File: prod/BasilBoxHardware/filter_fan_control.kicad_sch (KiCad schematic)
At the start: 4 parts, among them J1 FAN, U3 DEBO_Relais, U5 DEBO_Mosfet, U6 DEBO_Mosfet

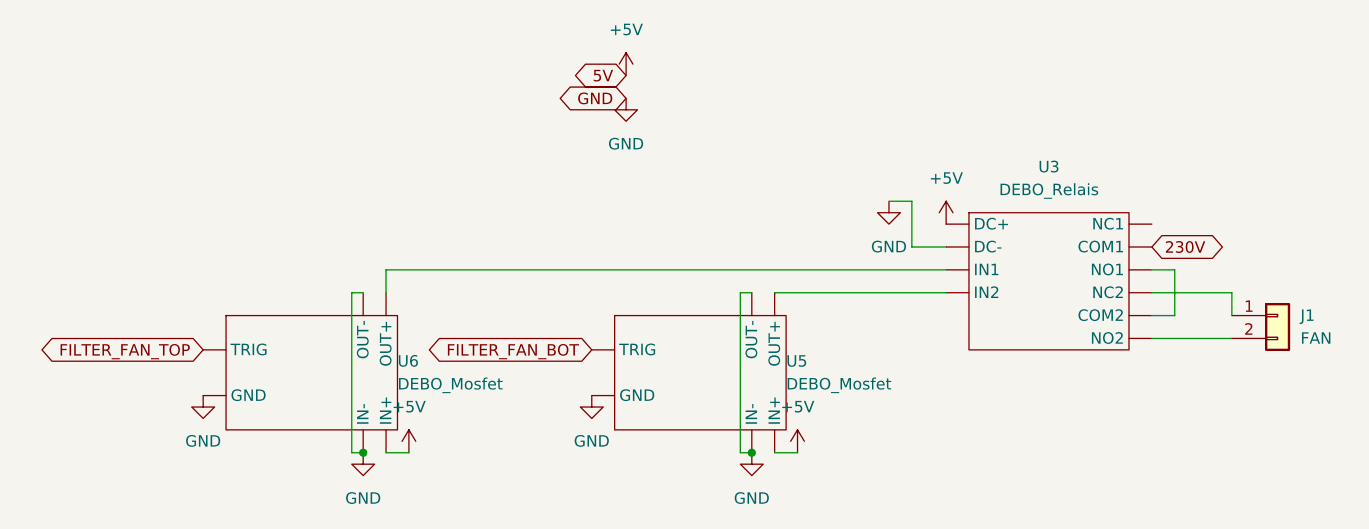
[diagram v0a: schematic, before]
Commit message: Add fan control and button handling
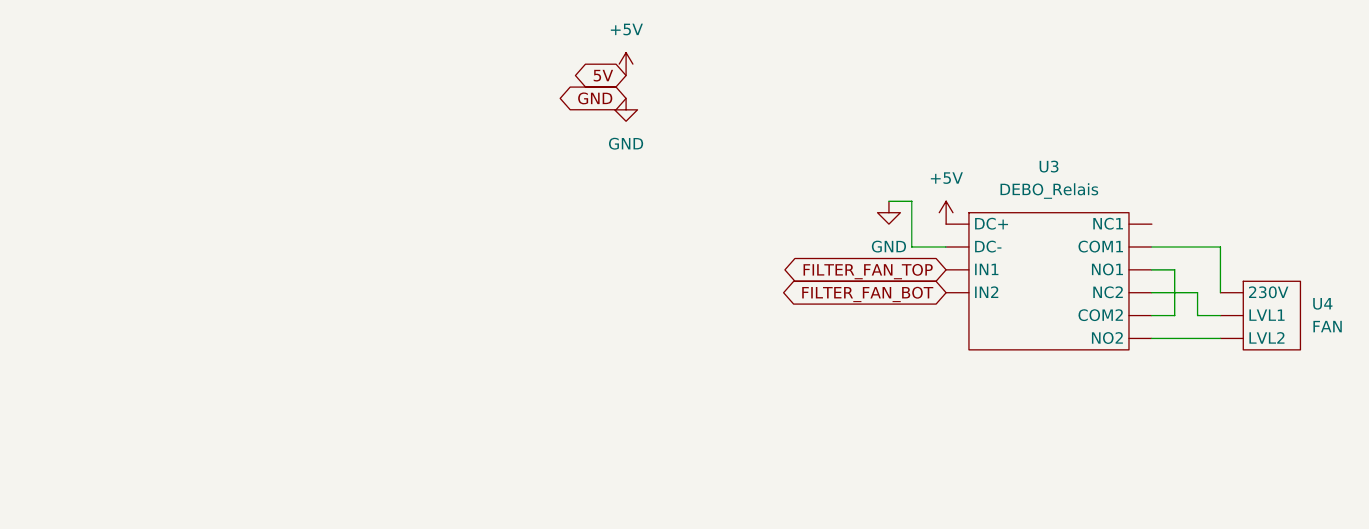
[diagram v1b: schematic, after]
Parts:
- removed J1: FAN, symbol Connector_Generic:Conn_01x02
- removed U5, U6: DEBO_Mosfet, symbol Driver_FET:DEBO_Mosfet
- added U4: FAN, symbol Motor:FAN
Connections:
- net 230V is gone; now on net GND: U3. (NO2)
- net FILTER_FAN_BOT: now also U3. (NO2)
- net FILTER_FAN_TOP: now also U3. (NO2)
- new net: U3. (NO2), U4. (LVL2) (x3)
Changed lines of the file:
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@@
 (kicad_sch (version 20211123) (generator eeschema)
   (paper "A4")
-  (junction (at 59.69 109.22) (diameter 0) (color 0 0 0 0)
-  )
-  (junction (at 102.87 109.22) (diameter 0) (color 0 0 0 0)
-  )
-  (wire (pts (xy 62.23 91.44) (xy 62.23 88.9))
-    (stroke (width 0) (type default) (color 0 0 0 0))
-  )
-  (wire (pts (xy 58.42 91.44) (xy 58.42 109.22))
-    (stroke (width 0) (type default) (color 0 0 0 0))
-  )
-  (wire (pts (xy 156.21 93.98) (xy 156.21 91.44))
-    (stroke (width 0) (type default) (color 0 0 0 0))
-  )
-  (wire (pts (xy 62.23 109.22) (xy 64.77 109.22))
+  (wire (pts (xy 147.32 86.36) (xy 154.94 86.36))
     (stroke (width 0) (type default) (color 0 0 0 0))
   )
@@
     (stroke (width 0) (type default) (color 0 0 0 0))
   )
-  (wire (pts (xy 59.69 91.44) (xy 58.42 91.44))
+  (wire (pts (xy 147.32 96.52) (xy 154.94 96.52))
     (stroke (width 0) (type default) (color 0 0 0 0))
   )
@@
     (stroke (width 0) (type default) (color 0 0 0 0))
   )
-  (wire (pts (xy 101.6 91.44) (xy 101.6 109.22))
+  (wire (pts (xy 152.4 93.98) (xy 154.94 93.98))
     (stroke (width 0) (type default) (color 0 0 0 0))
   )
@@
     (stroke (width 0) (type default) (color 0 0 0 0))
   )
-  (wire (pts (xy 156.21 91.44) (xy 147.32 91.44))
-    (stroke (width 0) (type default) (color 0 0 0 0))
-  )
-  (wire (pts (xy 105.41 109.22) (xy 107.95 109.22))
-    (stroke (width 0) (type default) (color 0 0 0 0))
-  )
-  (wire (pts (xy 105.41 91.44) (xy 124.46 91.44))
-    (stroke (width 0) (type default) (color 0 0 0 0))
-  )
-  (wire (pts (xy 101.6 109.22) (xy 102.87 109.22))
-    (stroke (width 0) (type default) (color 0 0 0 0))
-  )
-  (wire (pts (xy 58.42 109.22) (xy 59.69 109.22))
+  (wire (pts (xy 147.32 91.44) (xy 152.4 91.44))
     (stroke (width 0) (type default) (color 0 0 0 0))
   )
@@
     (stroke (width 0) (type default) (color 0 0 0 0))
   )
-  (wire (pts (xy 62.23 88.9) (xy 124.46 88.9))
+  (wire (pts (xy 152.4 91.44) (xy 152.4 93.98))
     (stroke (width 0) (type default) (color 0 0 0 0))
   )
-  (wire (pts (xy 147.32 96.52) (xy 156.21 96.52))
-    (stroke (width 0) (type default) (color 0 0 0 0))
-  )
-  (wire (pts (xy 102.87 91.44) (xy 101.6 91.44))
+  (wire (pts (xy 154.94 86.36) (xy 154.94 91.44))
     (stroke (width 0) (type default) (color 0 0 0 0))
   )
   (wire (pts (xy 124.46 86.36) (xy 120.65 86.36))
     (stroke (width 0) (type default) (color 0 0 0 0))
-  )
-  (global_label "230V" (shape bidirectional) (at 147.32 86.36 0) (fields_autoplaced)
-    (effects (font (size 1.27 1.27)) (justify left))
-    (property "Intersheet References" "${INTERSHEET_REFS}" (id 0) (at 154.4502 86.2806 0)
-      (effects (font (size 1.27 1.27)) (justify left) hide)
-    )
   )
   (global_label "GND" (shape bidirectional) (at 88.9 69.85 180) (fields_autoplaced)
@@
     )
   )
-  (global_label "FILTER_FAN_BOT" (shape bidirectional) (at 85.09 97.79 180) (fields_autoplaced)
+  (global_label "FILTER_FAN_BOT" (shape bidirectional) (at 124.46 91.44 180) (fields_autoplaced)
     (effects (font (size 1.27 1.27)) (justify right))
-    (property "Intersheet References" "${INTERSHEET_REFS}" (id 0) (at 67.5579 97.7106 0)
+    (property "Intersheet References" "${INTERSHEET_REFS}" (id 0) (at 106.9279 91.3606 0)
       (effects (font (size 1.27 1.27)) (justify right) hide)
     )
   )
-  (global_label "FILTER_FAN_TOP" (shape bidirectional) (at 41.91 97.79 180) (fields_autoplaced)
+  (global_label "FILTER_FAN_TOP" (shape bidirectional) (at 124.46 88.9 180) (fields_autoplaced)
     (effects (font (size 1.27 1.27)) (justify right))
-    (property "Intersheet References" "${INTERSHEET_REFS}" (id 0) (at 24.3779 97.7106 0)
+    (property "Intersheet References" "${INTERSHEET_REFS}" (id 0) (at 106.9279 88.8206 0)
       (effects (font (size 1.27 1.27)) (justify right) hide)
     )
@@
       (effects (font (size 1.27 1.27)) (justify right) hide)
     )
-  )
-  (symbol (lib_id "power:GND") (at 102.87 109.22 0) (unit 1)
-    (in_bom yes) (on_board yes) (fields_autoplaced)
-    (property "Reference" "#PWR?" (id 0) (at 102.87 115.57 0)
-      (effects (font (size 1.27 1.27)) hide)
-    )
-    (property "Value" "GND" (id 1) (at 102.87 114.3 0))
-    (property "Footprint" "" (id 2) (at 102.87 109.22 0)
-      (effects (font (size 1.27 1.27)) hide)
-    )
-    (property "Datasheet" "" (id 3) (at 102.87 109.22 0)
-      (effects (font (size 1.27 1.27)) hide)
-    )
-    (pin "1")
   )
   (symbol (lib_id "power:+5V") (at 124.46 83.82 0) (unit 1)
@@
     )
     (pin "1")
-  )
-  (symbol (lib_id "power:GND") (at 85.09 102.87 0) (unit 1)
-    (in_bom yes) (on_board yes) (fields_autoplaced)
-    (property "Reference" "#PWR?" (id 0) (at 85.09 109.22 0)
-      (effects (font (size 1.27 1.27)) hide)
-    )
-    (property "Value" "GND" (id 1) (at 85.09 107.95 0))
-    (property "Footprint" "" (id 2) (at 85.09 102.87 0)
-      (effects (font (size 1.27 1.27)) hide)
-    )
-    (property "Datasheet" "" (id 3) (at 85.09 102.87 0)
-      (effects (font (size 1.27 1.27)) hide)
-    )
-    (pin "1")
-  )
-  (symbol (lib_id "Driver_FET:DEBO_Mosfet") (at 44.45 93.98 0) (unit 1)
-    (in_bom yes) (on_board yes)
-    (property "Reference" "U6" (id 0) (at 63.5 99.06 0)
-      (effects (font (size 1.27 1.27)) (justify left))
-    )
-    (property "Value" "DEBO_Mosfet" (id 1) (at 63.5 101.6 0)
-      (effects (font (size 1.27 1.27)) (justify left))
-    )
-    (property "Footprint" "" (id 2) (at 44.45 93.98 0)
-      (effects (font (size 1.27 1.27)) hide)
-    )
-    (property "Datasheet" "" (id 3) (at 44.45 93.98 0)
-      (effects (font (size 1.27 1.27)) hide)
-    )
-    (pin "")
-    (pin "")
-    (pin "")
-    (pin "")
-    (pin "")
-    (pin "")
-  )
-  (symbol (lib_id "power:GND") (at 41.91 102.87 0) (unit 1)
-    (in_bom yes) (on_board yes) (fields_autoplaced)
-    (property "Reference" "#PWR?" (id 0) (at 41.91 109.22 0)
-      (effects (font (size 1.27 1.27)) hide)
-    )
-    (property "Value" "GND" (id 1) (at 41.91 107.95 0))
-    (property "Footprint" "" (id 2) (at 41.91 102.87 0)
-      (effects (font (size 1.27 1.27)) hide)
-    )
-    (property "Datasheet" "" (id 3) (at 41.91 102.87 0)
-      (effects (font (size 1.27 1.27)) hide)
-    )
-    (pin "1")
-  )
-  (symbol (lib_id "power:+5V") (at 107.95 109.22 0) (unit 1)
-    (in_bom yes) (on_board yes) (fields_autoplaced)
-    (property "Reference" "#PWR?" (id 0) (at 107.95 113.03 0)
-      (effects (font (size 1.27 1.27)) hide)
-    )
-    (property "Value" "+5V" (id 1) (at 107.95 104.14 0))
-    (property "Footprint" "" (id 2) (at 107.95 109.22 0)
-      (effects (font (size 1.27 1.27)) hide)
-    )
-    (property "Datasheet" "" (id 3) (at 107.95 109.22 0)
-      (effects (font (size 1.27 1.27)) hide)
-    )
-    (pin "1")
-  )
-  (symbol (lib_id "power:GND") (at 59.69 109.22 0) (unit 1)
-    (in_bom yes) (on_board yes) (fields_autoplaced)
-    (property "Reference" "#PWR?" (id 0) (at 59.69 115.57 0)
-      (effects (font (size 1.27 1.27)) hide)
-    )
-    (property "Value" "GND" (id 1) (at 59.69 114.3 0))
-    (property "Footprint" "" (id 2) (at 59.69 109.22 0)
-      (effects (font (size 1.27 1.27)) hide)
-    )
-    (property "Datasheet" "" (id 3) (at 59.69 109.22 0)
-      (effects (font (size 1.27 1.27)) hide)
-    )
-    (pin "1")
-  )
-  (symbol (lib_id "Driver_FET:DEBO_Mosfet") (at 87.63 93.98 0) (unit 1)
-    (in_bom yes) (on_board yes)
-    (property "Reference" "U5" (id 0) (at 106.68 99.06 0)
-      (effects (font (size 1.27 1.27)) (justify left))
-    )
-    (property "Value" "DEBO_Mosfet" (id 1) (at 106.68 101.6 0)
-      (effects (font (size 1.27 1.27)) (justify left))
-    )
-    (property "Footprint" "" (id 2) (at 87.63 93.98 0)
-      (effects (font (size 1.27 1.27)) hide)
-    )
-    (property "Datasheet" "" (id 3) (at 87.63 93.98 0)
-      (effects (font (size 1.27 1.27)) hide)
-    )
-    (pin "")
-    (pin "")
-    (pin "")
-    (pin "")
-    (pin "")
-    (pin "")
   )
   (symbol (lib_id "power:GND") (at 88.9 69.85 0) (unit 1)
@@
     (pin "1")
   )
-  (symbol (lib_id "power:+5V") (at 64.77 109.22 0) (unit 1)
+  (symbol (lib_id "Motor:FAN") (at 157.48 90.17 0) (unit 1)
     (in_bom yes) (on_board yes) (fields_autoplaced)
-    (property "Reference" "#PWR?" (id 0) (at 64.77 113.03 0)
+    (property "Reference" "U4" (id 0) (at 165.1 92.7099 0)
+      (effects (font (size 1.27 1.27)) (justify left))
+    )
+    (property "Value" "FAN" (id 1) (at 165.1 95.2499 0)
+      (effects (font (size 1.27 1.27)) (justify left))
+    )
+    (property "Footprint" "" (id 2) (at 157.48 90.17 0)
       (effects (font (size 1.27 1.27)) hide)
     )
-    (property "Value" "+5V" (id 1) (at 64.77 104.14 0))
-    (property "Footprint" "" (id 2) (at 64.77 109.22 0)
+    (property "Datasheet" "" (id 3) (at 157.48 90.17 0)
       (effects (font (size 1.27 1.27)) hide)
     )
-    (property "Datasheet" "" (id 3) (at 64.77 109.22 0)
-      (effects (font (size 1.27 1.27)) hide)
-    )
-    (pin "1")
+    (pin "")
+    (pin "")
+    (pin "")
   )
   (symbol (lib_id "Relay:DEBO_Relais") (at 127 82.55 0) (unit 1)
@@
     (pin "")
   )
-  (symbol (lib_id "Connector_Generic:Conn_01x02") (at 161.29 93.98 0) (unit 1)
-    (in_bom yes) (on_board yes) (fields_autoplaced)
-    (property "Reference" "J1" (id 0) (at 163.83 93.9799 0)
-      (effects (font (size 1.27 1.27)) (justify left))
-    )
-    (property "Value" "FAN" (id 1) (at 163.83 96.5199 0)
-      (effects (font (size 1.27 1.27)) (justify left))
-    )
-    (property "Footprint" "" (id 2) (at 161.29 93.98 0)
-      (effects (font (size 1.27 1.27)) hide)
-    )
-    (property "Datasheet" "~" (id 3) (at 161.29 93.98 0)
-      (effects (font (size 1.27 1.27)) hide)
-    )
-    (pin "1")
-    (pin "2")
-  )
 )

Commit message: Add led light control
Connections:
- new net: U3. (NO2), U4. (LVL2) (x2)

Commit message: Add hardware schematics
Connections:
- new net: U3. (NO2), U4. (LVL2) (x2)
